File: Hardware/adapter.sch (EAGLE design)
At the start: 6 parts

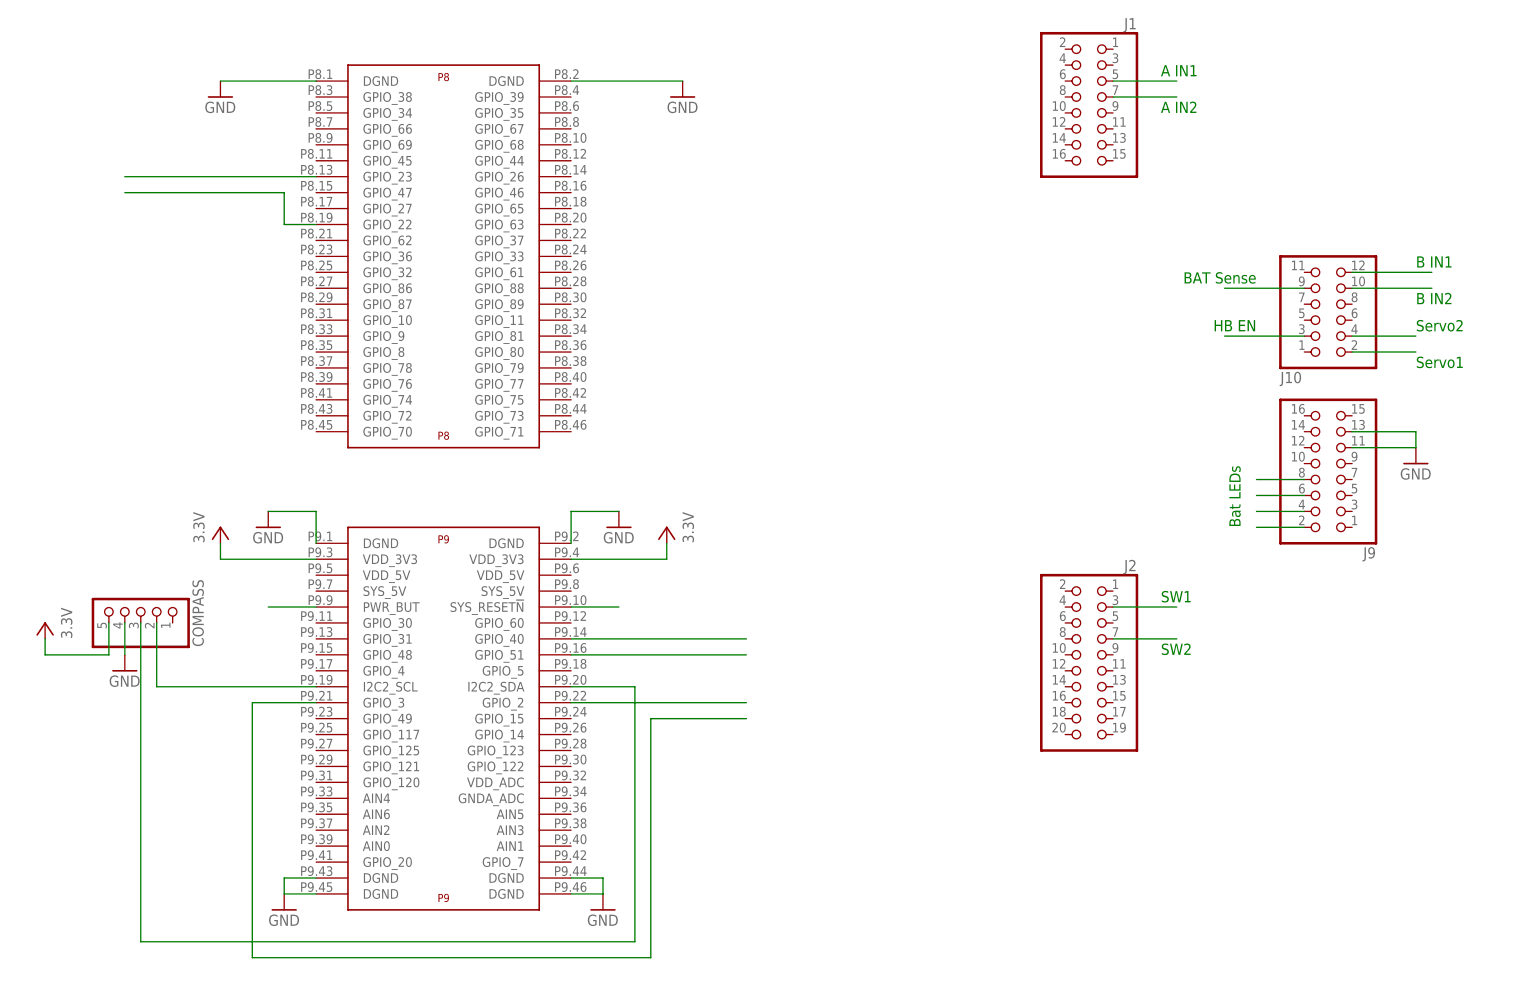
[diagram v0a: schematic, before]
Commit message: Added GPIO connections for switches and LEDs. Updated routing.
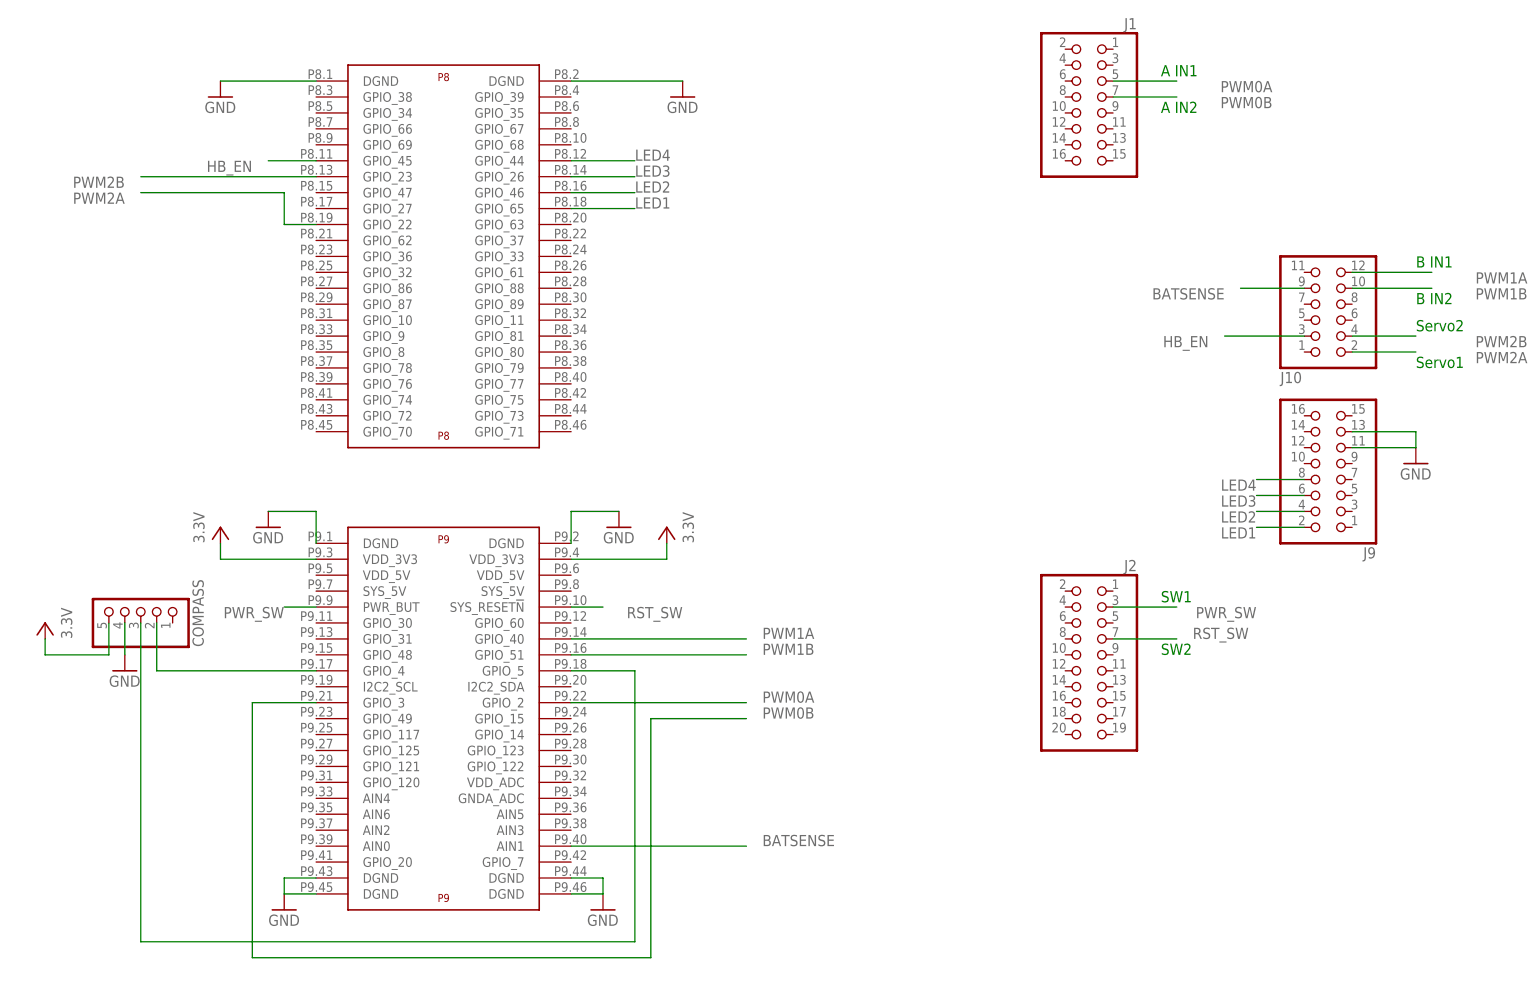
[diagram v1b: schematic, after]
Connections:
- removed net N$1: COMPASS.2, U$1P9.I2C2_SCL
- removed net N$2: COMPASS.3, U$1P9.I2C2_SDA
- removed net N$3: J10.9
- removed net N$4: J10.3
- removed net N$5: J9.2
- removed net N$6: J9.4
- removed net N$7: J9.6
- removed net N$8: J9.8
- new net BATSENSE: J10.9, U$1P9.AIN1
- new net HB_EN: J10.3, U$1P8.GPIO_45
- new net I2C1_SCL: COMPASS.2, U$1P9.GPIO_4
- new net I2C1_SDA: COMPASS.3, U$1P9.GPIO_5
- new net LED1: J9.2, U$1P8.GPIO_65
- new net LED2: J9.4, U$1P8.GPIO_46
- new net LED3: J9.6, U$1P8.GPIO_26
- new net LED4: J9.8, U$1P8.GPIO_44
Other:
- note removed: "BAT Sense"
- note removed: "Bat LEDs"
- note removed: "HB EN"
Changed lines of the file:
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@@
 <text x="132.08" y="40.64" size="1.778" layer="91" rot="MR180">SW1</text>
 <text x="132.08" y="30.48" size="1.778" layer="91">SW2</text>
-<text x="147.32" y="91.44" size="1.778" layer="91" rot="R180">BAT Sense</text>
-<text x="147.32" y="83.82" size="1.778" layer="91" rot="R180">HB EN</text>
-<text x="144.78" y="50.8" size="1.778" layer="91" rot="R90">Bat LEDs</text>
 </plain>
 <instances>
@@
 </segment>
 </net>
-<net name="N$1" class="0">
-<segment>
-<pinref part="U$1" gate="P9" pin="I2C2_SCL"/>
-<wire x1="-2.54" y1="25.4" x2="-27.94" y2="25.4" width="0.1524" layer="91"/>
+<net name="I2C1_SCL" class="0">
+<segment>
 <pinref part="COMPASS" gate="A" pin="2"/>
-<wire x1="-27.94" y1="25.4" x2="-27.94" y2="35.56" width="0.1524" layer="91"/>
-</segment>
-</net>
-<net name="N$2" class="0">
-<segment>
-<wire x1="48.26" y1="-15.24" x2="48.26" y2="25.4" width="0.1524" layer="91"/>
-<pinref part="U$1" gate="P9" pin="I2C2_SDA"/>
-<wire x1="48.26" y1="25.4" x2="38.1" y2="25.4" width="0.1524" layer="91"/>
-<pinref part="COMPASS" gate="A" pin="3"/>
-<wire x1="48.26" y1="-15.24" x2="-30.48" y2="-15.24" width="0.1524" layer="91"/>
-<wire x1="-30.48" y1="-15.24" x2="-30.48" y2="35.56" width="0.1524" layer="91"/>
+<wire x1="-27.94" y1="27.94" x2="-27.94" y2="35.56" width="0.1524" layer="91"/>
+<pinref part="U$1" gate="P9" pin="GPIO_4"/>
+<wire x1="-27.94" y1="27.94" x2="-2.54" y2="27.94" width="0.1524" layer="91"/>
 </segment>
 </net>
@@
 <pinref part="U$1" gate="P9" pin="GPIO_40"/>
 <wire x1="38.1" y1="33.02" x2="66.04" y2="33.02" width="0.1524" layer="91"/>
+<label x="68.58" y="33.02" size="1.778" layer="95"/>
 </segment>
 <segment>
 <pinref part="J10" gate="A" pin="12"/>
 <wire x1="162.56" y1="91.44" x2="175.26" y2="91.44" width="0.1524" layer="91"/>
+<label x="190.5" y="91.44" size="1.778" layer="95" rot="R180"/>
 </segment>
 </net>
@@
 <pinref part="U$1" gate="P9" pin="GPIO_51"/>
 <wire x1="38.1" y1="30.48" x2="66.04" y2="30.48" width="0.1524" layer="91"/>
+<label x="68.58" y="30.48" size="1.778" layer="95"/>
 </segment>
 <segment>
 <pinref part="J10" gate="A" pin="10"/>
 <wire x1="162.56" y1="88.9" x2="175.26" y2="88.9" width="0.1524" layer="91"/>
+<label x="190.5" y="88.9" size="1.778" layer="95" rot="R180"/>
 </segment>
 </net>
@@
 <pinref part="U$1" gate="P9" pin="GPIO_2"/>
 <wire x1="38.1" y1="22.86" x2="66.04" y2="22.86" width="0.1524" layer="91"/>
+<label x="68.58" y="22.86" size="1.778" layer="95"/>
 </segment>
 <segment>
 <wire x1="124.46" y1="121.92" x2="134.62" y2="121.92" width="0.1524" layer="91"/>
 <pinref part="J1" gate="A" pin="5"/>
+<label x="149.86" y="121.92" size="1.778" layer="95" rot="R180"/>
 </segment>
 </net>
@@
 <wire x1="50.8" y1="-17.78" x2="50.8" y2="20.32" width="0.1524" layer="91"/>
 <wire x1="50.8" y1="20.32" x2="66.04" y2="20.32" width="0.1524" layer="91"/>
+<label x="68.58" y="20.32" size="1.778" layer="95"/>
 </segment>
 <segment>
 <wire x1="124.46" y1="119.38" x2="134.62" y2="119.38" width="0.1524" layer="91"/>
 <pinref part="J1" gate="A" pin="7"/>
+<label x="149.86" y="119.38" size="1.778" layer="95" rot="R180"/>
 </segment>
 </net>
@@
 <segment>
 <pinref part="U$1" gate="P8" pin="GPIO_23"/>
-<wire x1="-2.54" y1="106.68" x2="-33.02" y2="106.68" width="0.1524" layer="91"/>
+<wire x1="-2.54" y1="106.68" x2="-30.48" y2="106.68" width="0.1524" layer="91"/>
+<label x="-33.02" y="106.68" size="1.778" layer="95" rot="R180"/>
 </segment>
 <segment>
 <pinref part="J10" gate="A" pin="4"/>
 <wire x1="162.56" y1="81.28" x2="172.72" y2="81.28" width="0.1524" layer="91"/>
+<label x="190.5" y="81.28" size="1.778" layer="95" rot="R180"/>
 </segment>
 </net>
@@
 <wire x1="-2.54" y1="99.06" x2="-7.62" y2="99.06" width="0.1524" layer="91"/>
 <wire x1="-7.62" y1="99.06" x2="-7.62" y2="104.14" width="0.1524" layer="91"/>
-<wire x1="-7.62" y1="104.14" x2="-33.02" y2="104.14" width="0.1524" layer="91"/>
+<wire x1="-7.62" y1="104.14" x2="-30.48" y2="104.14" width="0.1524" layer="91"/>
+<label x="-33.02" y="104.14" size="1.778" layer="95" rot="R180"/>
 </segment>
 <segment>
 <pinref part="J10" gate="A" pin="2"/>
 <wire x1="162.56" y1="78.74" x2="172.72" y2="78.74" width="0.1524" layer="91"/>
+<label x="190.5" y="78.74" size="1.778" layer="95" rot="R180"/>
 </segment>
 </net>
@@
 <pinref part="J2" gate="A" pin="3"/>
 <wire x1="124.46" y1="38.1" x2="134.62" y2="38.1" width="0.1524" layer="91"/>
+<label x="147.32" y="38.1" size="1.778" layer="95" rot="R180"/>
 </segment>
 <segment>
 <pinref part="U$1" gate="P9" pin="PWR_BUT"/>
-<wire x1="-2.54" y1="38.1" x2="-10.16" y2="38.1" width="0.1524" layer="91"/>
+<wire x1="-2.54" y1="38.1" x2="-7.62" y2="38.1" width="0.1524" layer="91"/>
+<label x="-7.62" y="38.1" size="1.778" layer="95" rot="R180"/>
 </segment>
 </net>
@@
 <pinref part="J2" gate="A" pin="7"/>
 <wire x1="124.46" y1="33.02" x2="134.62" y2="33.02" width="0.1524" layer="91"/>
+<label x="137.16" y="33.02" size="1.778" layer="95"/>
 </segment>
 <segment>
 <pinref part="U$1" gate="P9" pin="SYS_RESET!N"/>
-<wire x1="38.1" y1="38.1" x2="45.72" y2="38.1" width="0.1524" layer="91"/>
-</segment>
-</net>
-<net name="N$3" class="0">
+<wire x1="38.1" y1="38.1" x2="43.18" y2="38.1" width="0.1524" layer="91"/>
+<label x="55.88" y="38.1" size="1.778" layer="95" rot="R180"/>
+</segment>
+</net>
+<net name="BATSENSE" class="0">
 <segment>
 <pinref part="J10" gate="A" pin="9"/>
-<wire x1="154.94" y1="88.9" x2="142.24" y2="88.9" width="0.1524" layer="91"/>
-</segment>
-</net>
-<net name="N$4" class="0">
+<wire x1="154.94" y1="88.9" x2="144.78" y2="88.9" width="0.1524" layer="91"/>
+<label x="142.24" y="88.9" size="1.778" layer="95" rot="R180"/>
+</segment>
+<segment>
+<pinref part="U$1" gate="P9" pin="AIN1"/>
+<wire x1="38.1" y1="0" x2="66.04" y2="0" width="0.1524" layer="91"/>
+<label x="68.58" y="0" size="1.778" layer="95"/>
+</segment>
+</net>
+<net name="HB_EN" class="0">
 <segment>
 <pinref part="J10" gate="A" pin="3"/>
 <wire x1="154.94" y1="81.28" x2="142.24" y2="81.28" width="0.1524" layer="91"/>
-</segment>
-</net>
-<net name="N$5" class="0">
+<label x="139.7" y="81.28" size="1.778" layer="95" rot="R180"/>
+</segment>
+<segment>
+<pinref part="U$1" gate="P8" pin="GPIO_45"/>
+<wire x1="-2.54" y1="109.22" x2="-10.16" y2="109.22" width="0.1524" layer="91"/>
+<label x="-12.7" y="109.22" size="1.778" layer="95" rot="R180"/>
+</segment>
+</net>
+<net name="I2C1_SDA" class="0">
+<segment>
+<pinref part="COMPASS" gate="A" pin="3"/>
+<wire x1="-30.48" y1="35.56" x2="-30.48" y2="-15.24" width="0.1524" layer="91"/>
+<wire x1="-30.48" y1="-15.24" x2="48.26" y2="-15.24" width="0.1524" layer="91"/>
+<wire x1="48.26" y1="-15.24" x2="48.26" y2="27.94" width="0.1524" layer="91"/>
+<pinref part="U$1" gate="P9" pin="GPIO_5"/>
+<wire x1="48.26" y1="27.94" x2="38.1" y2="27.94" width="0.1524" layer="91"/>
+</segment>
+</net>
+<net name="LED1" class="0">
 <segment>
 <wire x1="154.94" y1="50.8" x2="147.32" y2="50.8" width="0.1524" layer="91"/>
 <pinref part="J9" gate="A" pin="2"/>
-</segment>
-</net>
-<net name="N$6" class="0">
+<label x="147.32" y="50.8" size="1.778" layer="95" rot="R180"/>
+</segment>
+<segment>
+<pinref part="U$1" gate="P8" pin="GPIO_65"/>
+<wire x1="38.1" y1="101.6" x2="48.26" y2="101.6" width="0.1524" layer="91"/>
+<label x="48.26" y="101.6" size="1.778" layer="95"/>
+</segment>
+</net>
+<net name="LED2" class="0">
 <segment>
 <wire x1="154.94" y1="53.34" x2="147.32" y2="53.34" width="0.1524" layer="91"/>
 <pinref part="J9" gate="A" pin="4"/>
-</segment>
-</net>
-<net name="N$7" class="0">
+<label x="147.32" y="53.34" size="1.778" layer="95" rot="R180"/>
+</segment>
+<segment>
+<pinref part="U$1" gate="P8" pin="GPIO_46"/>
+<wire x1="38.1" y1="104.14" x2="48.26" y2="104.14" width="0.1524" layer="91"/>
+<label x="48.26" y="104.14" size="1.778" layer="95"/>
+</segment>
+</net>
+<net name="LED3" class="0">
 <segment>
 <wire x1="154.94" y1="55.88" x2="147.32" y2="55.88" width="0.1524" layer="91"/>
 <pinref part="J9" gate="A" pin="6"/>
-</segment>
-</net>
-<net name="N$8" class="0">
+<label x="147.32" y="55.88" size="1.778" layer="95" rot="R180"/>
+</segment>
+<segment>
+<pinref part="U$1" gate="P8" pin="GPIO_26"/>
+<wire x1="38.1" y1="106.68" x2="48.26" y2="106.68" width="0.1524" layer="91"/>
+<label x="48.26" y="106.68" size="1.778" layer="95"/>
+</segment>
+</net>
+<net name="LED4" class="0">
 <segment>
 <wire x1="154.94" y1="58.42" x2="147.32" y2="58.42" width="0.1524" layer="91"/>
 <pinref part="J9" gate="A" pin="8"/>
-</segment>
-</net>
+<label x="147.32" y="58.42" size="1.778" layer="95" rot="R180"/>
+</segment>
+<segment>
+<pinref part="U$1" gate="P8" pin="GPIO_44"/>
+<wire x1="38.1" y1="109.22" x2="48.26" y2="109.22" width="0.1524" layer="91"/>
+<label x="48.26" y="109.22" size="1.778" layer="95"/>
+</segment>
+</net>
